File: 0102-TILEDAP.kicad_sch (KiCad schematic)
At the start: 39 parts

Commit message: Update gerber V1.2
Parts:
- C1, C3: value (none) -> 10uF/25V; footprint (none) -> Capacitor_SMD:C_0805_2012Metric
- C11, C8: value (none) -> 22pF; footprint (none) -> Capacitor_SMD:C_0402_1005Metric
- C12, C13, C4, C5, C6, C7: value (none) -> 100nF; footprint (none) -> Capacitor_SMD:C_0402_1005Metric
- C2: value (none) -> 10nF; footprint (none) -> Capacitor_SMD:C_0402_1005Metric
- D1: value (none) -> BLUE; footprint (none) -> LED_SMD:LED_0603_1608Metric
- D3: value (none) -> RED; footprint (none) -> LED_SMD:LED_0603_1608Metric
- H1, H2, H3: value (none) -> MountingHole; footprint (none) -> MountingHole:MountingHole_2.2mm_M2
- J1: value (none) -> USB-C; footprint (none) -> JLC-SMT:KINGHELM_KH-TYPE-C-L10-14P
- J2: value (none) -> IF; footprint (none) -> Connector_PinHeader_1.27mm:PinHeader_1x04_P1.27mm_Vertical
- J3: value (none) -> TGT; footprint (none) -> Connector_PinHeader_2.54mm:PinHeader_2x05_P2.54mm_Vertical
- Q1: value (none) -> S8550; footprint (none) -> Package_TO_SOT_SMD:SOT-23
- R1, R3: value (none) -> 5.1K; footprint (none) -> Resistor_SMD:R_0402_1005Metric
- R10, R11, R14: value (none) -> 1.5K; footprint (none) -> Resistor_SMD:R_0402_1005Metric
- R12, R2: value (none) -> 10K; footprint (none) -> Resistor_SMD:R_0402_1005Metric
- R13, R8: value (none) -> 100K; footprint (none) -> Resistor_SMD:R_0402_1005Metric
- R15: value (none) -> 470R; footprint (none) -> Resistor_SMD:R_0402_1005Metric
- R4, R5: value (none) -> 0R; footprint (none) -> Resistor_SMD:R_0402_1005Metric
- R6, R7: value (none) -> 4.7K; footprint (none) -> Resistor_SMD:R_0402_1005Metric
- R9: value (none) -> 100R; footprint (none) -> Resistor_SMD:R_0402_1005Metric
- SW1: value (none) -> SW_Push; footprint (none) -> JLC-SMT:HCTL_TC-3601L-2.5
- U1: value (none) -> SPX3819M5-L-3-3; footprint (none) -> Package_TO_SOT_SMD:SOT-23-5
- U2: value (none) -> STM32F103TBU6; footprint (none) -> Package_DFN_QFN:QFN-36-1EP_6x6mm_P0.5mm_EP4.1x4.1mm
- Y1: value (none) -> 8MHz; footprint (none) -> JLC-SMT:Oscillator_SMD_3.2x2.5mm

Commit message: Fix USB_ENUM
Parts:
- Q1: symbol Transistor_BJT:S8550 -> Device:Q_PNP_BEC
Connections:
- net +3V3: now also Q1.2 (E); no longer Q1.1 (E)
- net at R14.2: now also Q1.1 (B); no longer Q1.2 (B)
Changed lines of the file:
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@@
     (pin "1")
   )
-  (symbol (lib_id "Transistor_BJT:S8550") (at 73.66 33.02 180) (unit 1)
+  (symbol (lib_id "Device:Q_PNP_BEC") (at 73.66 33.02 180) (unit 1)
     (in_bom yes) (on_board yes)
     (property "Reference" "Q1" (id 0) (at 68.8086 31.8516 0)
@@
       (effects (font (size 1.27 1.27)) (justify left))
     )
-    (property "Footprint" "Package_TO_SOT_SMD:SOT-23" (id 2) (at 68.58 31.115 0)
-      (effects (font (size 1.27 1.27) italic) (justify left) hide)
+    (property "Footprint" "Package_TO_SOT_SMD:SOT-23" (id 2) (at 68.58 35.56 0)
+      (effects (font (size 1.27 1.27)) hide)
     )
-    (property "Datasheet" "http://www.unisonic.com.tw/datasheet/S8550.pdf" (id 3) (at 73.66 33.02 0)
-      (effects (font (size 1.27 1.27)) (justify left) hide)
+    (property "Datasheet" "~" (id 3) (at 73.66 33.02 0)
+      (effects (font (size 1.27 1.27)) hide)
     )
     (property "Manufacturer" "CJ" (id 4) (at 73.66 33.02 0)

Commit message: Update resistor for LED_CON_BLUE
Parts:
- R11: value 1.5K -> 220R; PartNumber C25867 -> C25091
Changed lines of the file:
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@@
     (in_bom yes) (on_board yes)
     (property "Reference" "R11" (id 0) (at 52.07 159.893 90))
-    (property "Value" "1.5K" (id 1) (at 52.07 162.2044 90))
+    (property "Value" "220R" (id 1) (at 52.07 162.2044 90))
     (property "Footprint" "Resistor_SMD:R_0402_1005Metric" (id 2) (at 51.816 166.116 90)
       (effects (font (size 1.27 1.27)) hide)
@@
       (effects (font (size 1.27 1.27)) hide)
     )
-    (property "PartNumber" "C25867" (id 5) (at 52.07 165.1 0)
+    (property "PartNumber" "C25091" (id 5) (at 52.07 165.1 0)
       (effects (font (size 1.27 1.27)) hide)
     )
@@
     )
     (path "/00000000-0000-0000-0000-0000630e036e"
-      (reference "R11") (unit 1) (value "1.5K") (footprint "Resistor_SMD:R_0402_1005Metric")
+      (reference "R11") (unit 1) (value "220R") (footprint "Resistor_SMD:R_0402_1005Metric")
     )
     (path "/00000000-0000-0000-0000-0000630ad8fe"

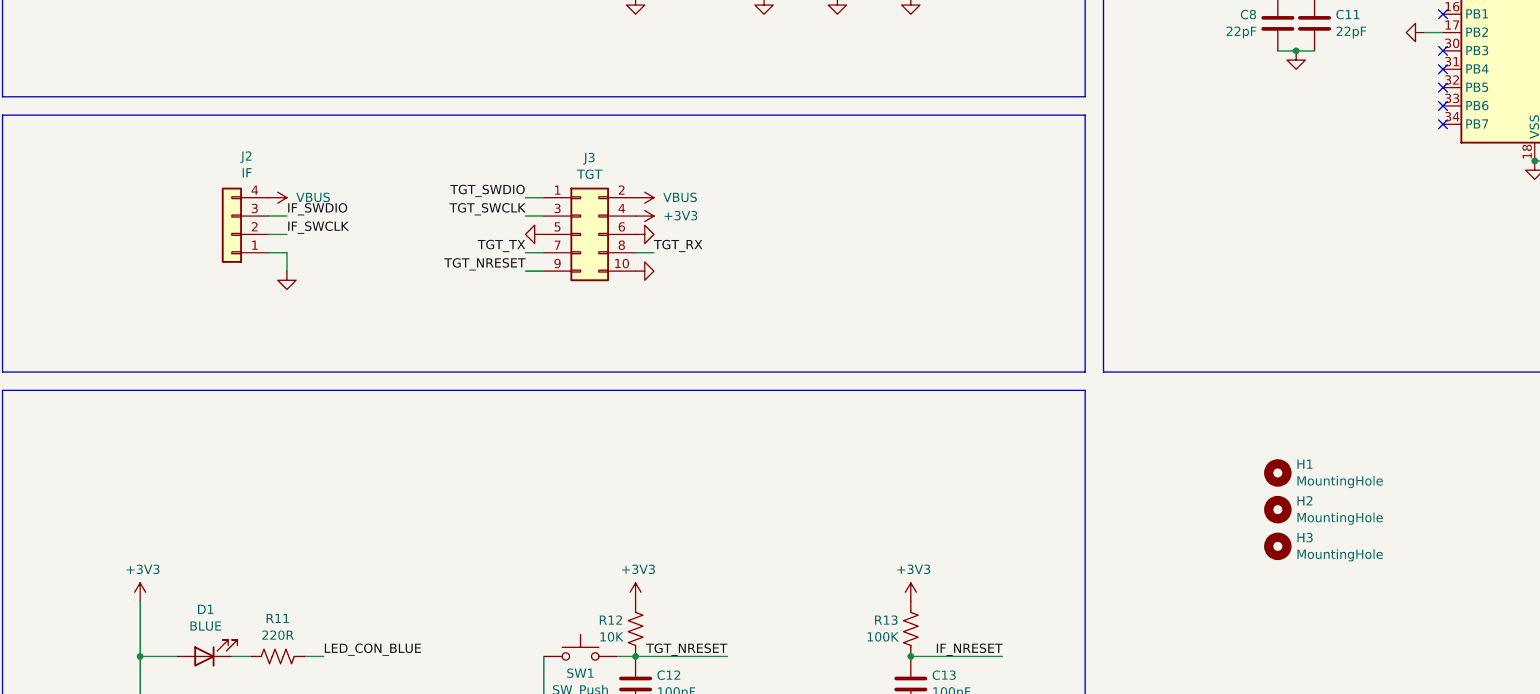
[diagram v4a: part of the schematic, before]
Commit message: Rework PCB
* Use New boundary
* Use laid USB-C connector
* Add ESDs
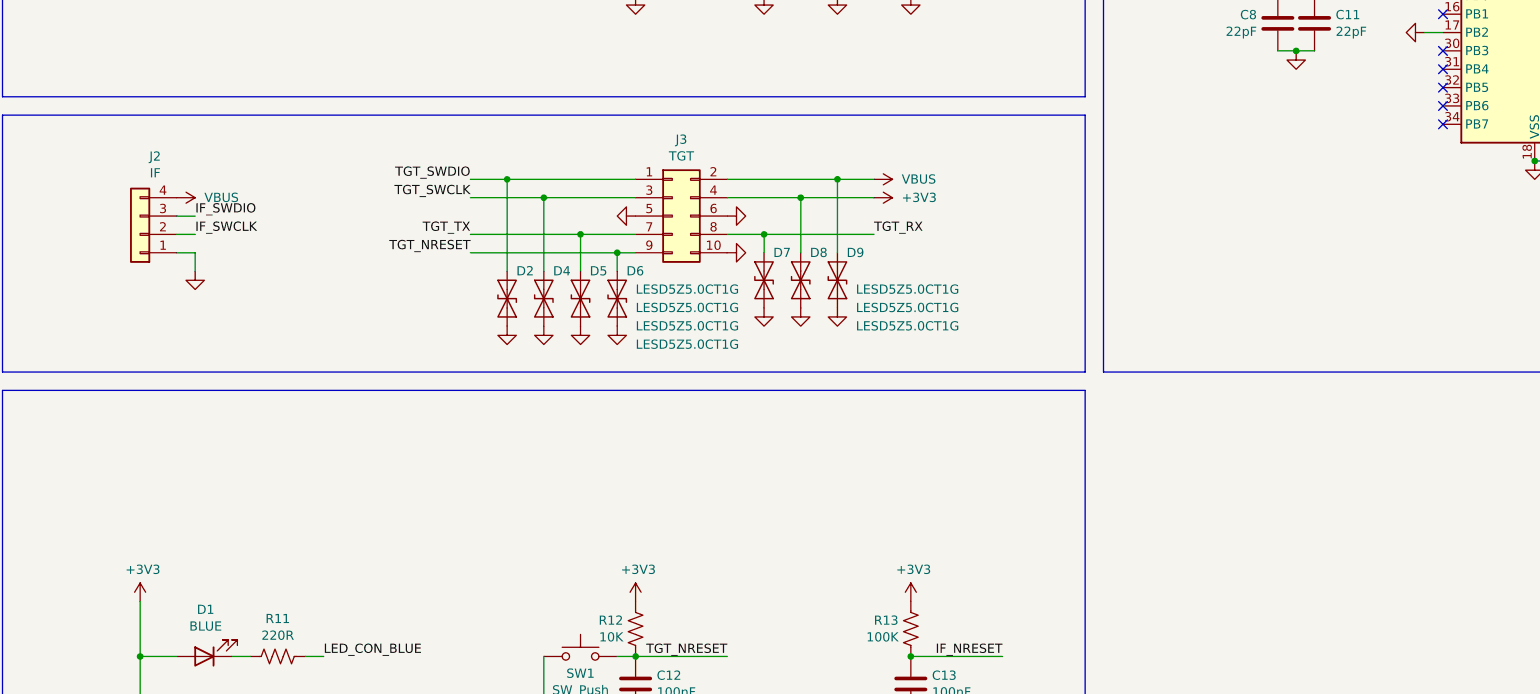
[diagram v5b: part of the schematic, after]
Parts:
- removed H1, H2, H3: MountingHole, MountingHole:MountingHole_2.2mm_M2, symbol Mechanical:MountingHole
- added D2, D4, D5, D6, D7, D8, D9: LESD5Z5.0CT1G, Diode_SMD:D_SOD-523, symbol Diode:ESD9B5.0ST5G
- J1: footprint JLC-SMT:KINGHELM_KH-TYPE-C-L10-14P -> JLC-SMT:HRO_TYPE-C-31-M-12; Manufacturer kinghelm -> HRO; PartNumber C2761226 -> C165948
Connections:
- net +3V3: now also D8.2 (A2)
- net GND: now also D2.1 (A1), D4.1 (A1), D5.1 (A1), D6.1 (A1), D7.1 (A1), D8.1 (A1), D9.1 (A1)
- net TGT_NRESET: now also D6.2 (A2)
- net TGT_RX: now also D7.2 (A2)
- net TGT_SWCLK: now also D4.2 (A2)
- net TGT_SWDIO: now also D2.2 (A2)
- net TGT_TX: now also D5.2 (A2)
- net VBUS: now also D9.2 (A2)
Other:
- moved on the sheet: J2, J3
